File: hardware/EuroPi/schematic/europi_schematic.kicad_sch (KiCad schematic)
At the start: 109 parts, among them J1 Output 1 Jack, J2 Output 2 Jack, J3 Output 3 Jack, J4 Output 4 Jack, J5 Output 5 Jack, J6 Output 6 Jack, J7 Digital Input Jack, J8 Analogue Input Jack, Q1 2N2222, SW1 SW_Push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

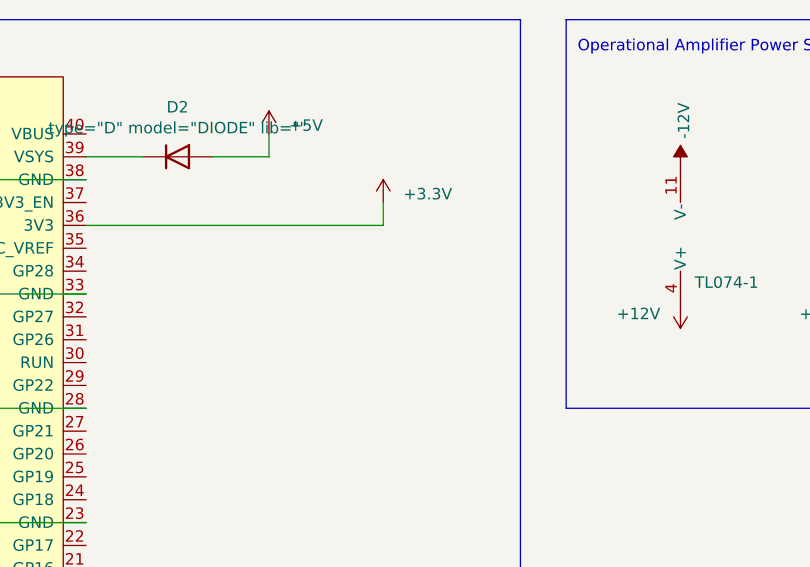
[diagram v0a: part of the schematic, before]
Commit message: add c1 to schematic file and pdf
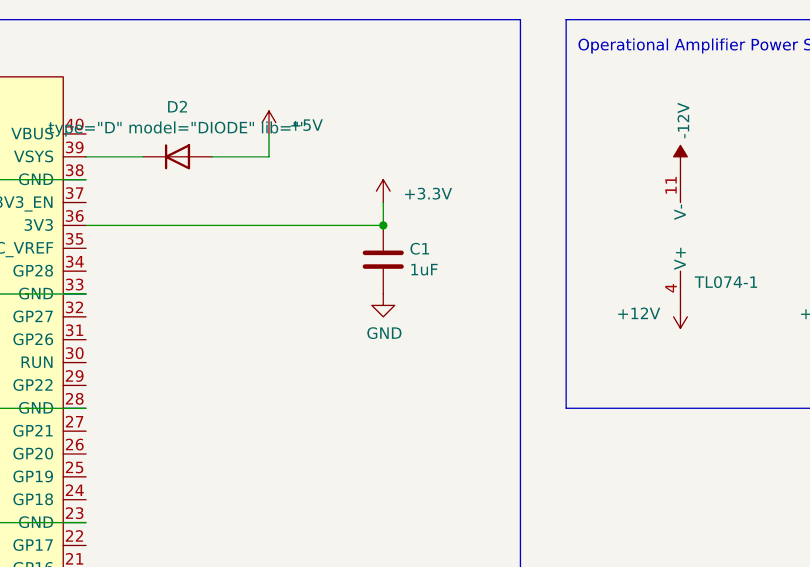
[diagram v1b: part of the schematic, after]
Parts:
- added C1: 1uF, symbol Device:C
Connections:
- net GND: now also C1.2
- net at Reference?.1, U?.36 (3V3): now also C1.1
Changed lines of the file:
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@@
   (junction (at 115.57 170.18) (diameter 0) (color 0 0 0 0)
   )
+  (junction (at 111.76 227.33) (diameter 0) (color 0 0 0 0)
+  )
   (junction (at 358.14 175.26) (diameter 0) (color 0 0 0 0)
   )
@@
         )
       )
+    )
+  )
+  (symbol (lib_id "power:GND") (at 111.76 234.95 0) (unit 1)
+    (in_bom yes) (on_board yes) (dnp no)
+    (property "Reference" "#PWR01" (at 111.76 241.3 0)
+      (effects (font (size 1.27 1.27)) hide)
+    )
+    (property "Value" "GND" (at 111.887 239.3442 0)
+      (effects (font (size 1.27 1.27)))
+    )
+    (property "Footprint" "" (at 111.76 234.95 0)
+      (effects (font (size 1.27 1.27)) hide)
+    )
+    (property "Datasheet" "" (at 111.76 234.95 0)
+      (effects (font (size 1.27 1.27)) hide)
+    )
+    (pin "1")
+    (instances
+      (project "europi_schematic"
+        (path "/5701b80f-f006-4814-81c9-0c7f006088a9"
+          (reference "#PWR01") (unit 1)
+        )
+      )
+    )
+  )
+  (symbol (lib_id "Device:C") (at 111.76 231.14 0) (unit 1)
+    (in_bom yes) (on_board yes) (dnp no)
+    (property "Reference" "C1" (at 114.681 229.9716 0)
+      (effects (font (size 1.27 1.27)) (justify left))
+    )
+    (property "Value" "1uF" (at 114.681 232.283 0)
+      (effects (font (size 1.27 1.27)) (justify left))
+    )
+    (property "Footprint" "" (at 112.7252 234.95 0)
+      (effects (font (size 1.27 1.27)) hide)
+    )
+    (property "Datasheet" "~" (at 111.76 231.14 0)
+      (effects (font (size 1.27 1.27)) hide)
+    )
+    (pin "1")
+    (pin "2")
+    (instances
+      (project "europi_schematic"
+        (path "/5701b80f-f006-4814-81c9-0c7f006088a9"
+          (reference "C1") (unit 1)
+        )
+      )
